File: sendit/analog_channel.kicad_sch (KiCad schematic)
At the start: 21 parts, among them J2 Conn_01x03, J4 JUMPER, J5 Conn_02x05_Odd_Even, J6 JUMPER, J7 Conn_02x05_Odd_Even, J8 JUMPER

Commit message: more work on rev c board schematic
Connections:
- net EXTERN renamed VEXT
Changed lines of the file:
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@@
 	(wire
 		(pts
-			(xy 85.09 60.96) (xy 85.09 71.12)
+			(xy 85.09 62.23) (xy 85.09 71.12)
 		)
 		(stroke
@@
 			(width 0)
 			(type default)
-		)
-	)
-	(global_label "EXTERN"
-		(shape input)
-		(at 85.09 60.96 90)
-		(fields_autoplaced yes)
-		(effects
-			(font
-				(size 1.27 1.27)
-			)
-			(justify left)
-		)
-		(property "Intersheetrefs" "${INTERSHEET_REFS}"
-			(at 85.09 50.8992 90)
-			(effects
-				(font
-					(size 1.27 1.27)
-				)
-				(justify left)
-			)
 		)
 	)
@@
 					(unit 1)
 				)
+			)
+		)
+	)
+	(symbol
+		(lib_id "power:VS")
+		(at 85.09 62.23 0)
+		(unit 1)
+		(exclude_from_sim no)
+		(in_bom yes)
+		(on_board yes)
+		(dnp no)
+		(fields_autoplaced yes)
+		(property "Reference" "#PWR0111"
+			(at 85.09 66.04 0)
+			(effects
+				(font
+					(size 1.27 1.27)
+				)
+				(hide yes)
+			)
+		)
+		(property "Value" "VEXT"
+			(at 85.09 57.15 0)
+			(effects
+				(font
+					(size 1.27 1.27)
+				)
+			)
+		)
+		(property "Footprint" ""
+			(at 85.09 62.23 0)
+			(effects
+				(font
+					(size 1.27 1.27)
+				)
+				(hide yes)
+			)
+		)
+		(property "Datasheet" ""
+			(at 85.09 62.23 0)
+			(effects
+				(font
+					(size 1.27 1.27)
+				)
+				(hide yes)
+			)
+		)
+		(property "Description" "Power symbol creates a global label with name \"VS\""
+			(at 85.09 62.23 0)
+			(effects
+				(font
+					(size 1.27 1.27)
+				)
+				(hide yes)
+			)
+		)
+		(pin "1"
+		)
+		(instances
+			(project "sendit"
+				(path "/a355e4d0-2918-44fc-be8d-2503b84c6d6c/06289466-09ce-4e8d-a3fe-f20bb105c2b9"
+					(reference "#PWR0114")
+					(unit 1)
+				)
+				(path "/a355e4d0-2918-44fc-be8d-2503b84c6d6c/5dcf4aa4-b4c0-4eb4-9810-8e1da6fba809"
+					(reference "#PWR0112")
+					(unit 1)
+				)
+				(path "/a355e4d0-2918-44fc-be8d-2503b84c6d6c/81493a67-66de-41a8-9145-e2b5bf5e8fe3"
+					(reference "#PWR0117")
+					(unit 1)
+				)
+				(path "/a355e4d0-2918-44fc-be8d-2503b84c6d6c/8214e645-c73d-48c5-bbb1-69f276b453fe"
+					(reference "#PWR0113")
+					(unit 1)
+				)
+				(path "/a355e4d0-2918-44fc-be8d-2503b84c6d6c/9719621a-b94a-4b2b-95d3-3cdc5abcb21e"
+					(reference "#PWR0118")
+					(unit 1)
+				)
+				(path "/a355e4d0-2918-44fc-be8d-2503b84c6d6c/d62eac9c-79f7-42c7-961a-243a4f5db43f"
+					(reference "#PWR0111")
+					(unit 1)
+				)
+				(path "/a355e4d0-2918-44fc-be8d-2503b84c6d6c/dea3d2e6-dd3a-44c1-a00c-3b7e188a1340"
+					(reference "#PWR0115")
+					(unit 1)
+				)
+				(path "/a355e4d0-2918-44fc-be8d-2503b84c6d6c/edcf8ea2-5577-432a-b9e3-a0cdd8283da4"
+					(reference "#PWR0116")
+					(unit 1)
+				)

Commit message: most of the work on the schematic is done.
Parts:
- renumbered TP1 to TP3, TP2 to TP4

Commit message: more work towards rev c board.
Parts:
- renumbered INPUT2 to INPUT1, J2 to J1, J3 to J2, J4 to J3, J5 to J4, J6 to J5, J7 to J6, J8 to J7, R1 to R3, R2 to R4, R3 to R5, R4 to R6, R5 to R7, R6 to R8, R7 to R9

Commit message: power system work and layout
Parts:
- renumbered J1 to J2, J2 to J3, J3 to J4, J4 to J5, J5 to J6, J6 to J7, J7 to J8

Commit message: big change removing the usb hub and serial chip.
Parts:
- renumbered J2 to J3, J3 to J4, J4 to J5, J5 to J6, J6 to J7, J7 to J8, J8 to J9

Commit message: big routing push
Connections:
- net +24V: now also J4.4 (Pin_4); no longer J4.6 (Pin_6)
- net +3.3VADC: now also J4.8 (Pin_8); no longer J4.2 (Pin_2)
- net +5V: now also J4.6 (Pin_6); no longer J4.4 (Pin_4)
- net VEXT: now also J4.2 (Pin_2); no longer J4.8 (Pin_8)
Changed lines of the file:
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@@
 	(wire
 		(pts
-			(xy 60.96 66.04) (xy 72.39 66.04)
+			(xy 60.96 66.04) (xy 71.12 66.04)
 		)
 		(stroke
@@
 	(wire
 		(pts
-			(xy 72.39 62.23) (xy 72.39 66.04)
+			(xy 71.12 62.23) (xy 71.12 66.04)
 		)
 		(stroke
@@
 	(wire
 		(pts
-			(xy 78.74 62.23) (xy 78.74 68.58)
+			(xy 77.47 62.23) (xy 77.47 68.58)
 		)
 		(stroke
@@
 	(wire
 		(pts
-			(xy 60.96 68.58) (xy 78.74 68.58)
+			(xy 60.96 68.58) (xy 77.47 68.58)
 		)
 		(stroke
@@
 	(symbol
 		(lib_id "power:+24V")
-		(at 78.74 62.23 0)
+		(at 71.12 62.23 0)
 		(unit 1)
 		(exclude_from_sim no)
@@
 		(fields_autoplaced yes)
 		(property "Reference" "#PWR019"
-			(at 78.74 66.04 0)
+			(at 71.12 66.04 0)
 			(effects
 				(font
@@
 		)
 		(property "Value" "+24V"
-			(at 78.74 57.15 0)
+			(at 71.12 57.15 0)
 			(effects
 				(font
@@
 		)
 		(property "Footprint" ""
-			(at 78.74 62.23 0)
+			(at 71.12 62.23 0)
 			(effects
 				(font
@@
 		)
 		(property "Datasheet" ""
-			(at 78.74 62.23 0)
+			(at 71.12 62.23 0)
 			(effects
 				(font
@@
 		)
 		(property "Description" "Power symbol creates a global label with name \"+24V\""
-			(at 78.74 62.23 0)
+			(at 71.12 62.23 0)
 			(effects
 				(font
@@
 	(symbol
 		(lib_id "power:+3.3VADC")
-		(at 64.77 62.23 0)
+		(at 85.09 62.23 0)
 		(mirror y)
 		(unit 1)
@@
 		(dnp no)
 		(property "Reference" "#PWR017"
-			(at 60.96 63.5 0)
+			(at 81.28 63.5 0)
 			(effects
 				(font
@@
 		)
 		(property "Value" "+3.3VADC"
-			(at 64.77 57.15 0)
+			(at 85.09 57.15 0)
 			(effects
 				(font
@@
 		)
 		(property "Footprint" ""
-			(at 64.77 62.23 0)
+			(at 85.09 62.23 0)
 			(effects
 				(font
@@
 		)
 		(property "Datasheet" ""
-			(at 64.77 62.23 0)
+			(at 85.09 62.23 0)
 			(effects
 				(font
@@
 		)
 		(property "Description" "Power symbol creates a global label with name \"+3.3VADC\""
-			(at 64.77 62.23 0)
+			(at 85.09 62.23 0)
 			(effects
 				(font
@@
 	(symbol
 		(lib_id "power:+5V")
-		(at 72.39 62.23 0)
+		(at 77.47 62.23 0)
 		(unit 1)
 		(exclude_from_sim no)
@@
 		(fields_autoplaced yes)
 		(property "Reference" "#PWR018"
-			(at 72.39 66.04 0)
+			(at 77.47 66.04 0)
 			(effects
 				(font
@@
 		)
 		(property "Value" "+5V"
-			(at 72.39 57.15 0)
+			(at 77.47 57.15 0)
 			(effects
 				(font
@@
 		)
 		(property "Footprint" ""
-			(at 72.39 62.23 0)
+			(at 77.47 62.23 0)
 			(effects
 				(font
@@
 		)
 		(property "Datasheet" ""
-			(at 72.39 62.23 0)
+			(at 77.47 62.23 0)
 			(effects
 				(font
@@
 		)
 		(property "Description" "Power symbol creates a global label with name \"+5V\""
-			(at 72.39 62.23 0)
+			(at 77.47 62.23 0)
 			(effects
 				(font
@@
 	(symbol
 		(lib_id "power:VS")
-		(at 85.09 62.23 0)
+		(at 64.77 62.23 0)
 		(unit 1)
 		(exclude_from_sim no)
@@
 		(fields_autoplaced yes)
 		(property "Reference" "#PWR020"
-			(at 85.09 66.04 0)
+			(at 64.77 66.04 0)
 			(effects
 				(font
@@
 		)
 		(property "Value" "VEXT"
-			(at 85.09 57.15 0)
+			(at 64.77 57.15 0)
 			(effects
 				(font
@@
 		)
 		(property "Footprint" ""
-			(at 85.09 62.23 0)
+			(at 64.77 62.23 0)
 			(effects
 				(font
@@
 		)
 		(property "Datasheet" ""
-			(at 85.09 62.23 0)
+			(at 64.77 62.23 0)
 			(effects
 				(font
@@
 		)
 		(property "Description" "Power symbol creates a global label with name \"VS\""
-			(at 85.09 62.23 0)
+			(at 64.77 62.23 0)
 			(effects
 				(font

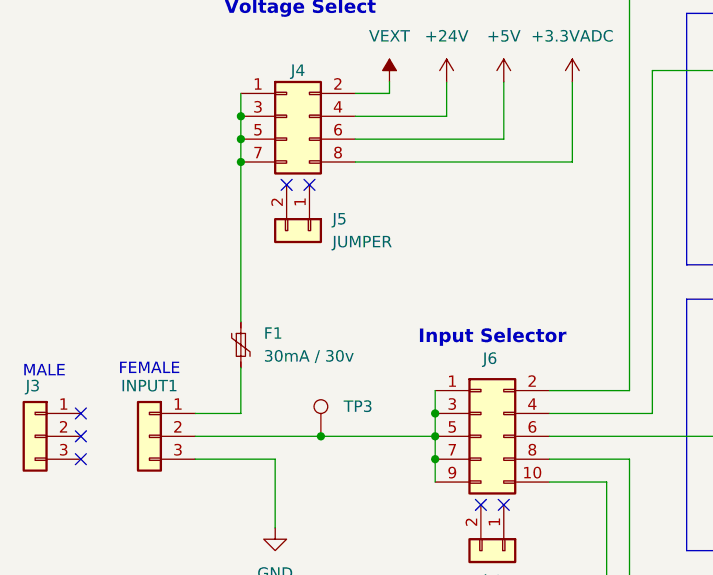
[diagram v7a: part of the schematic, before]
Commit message: via stitching and calculations
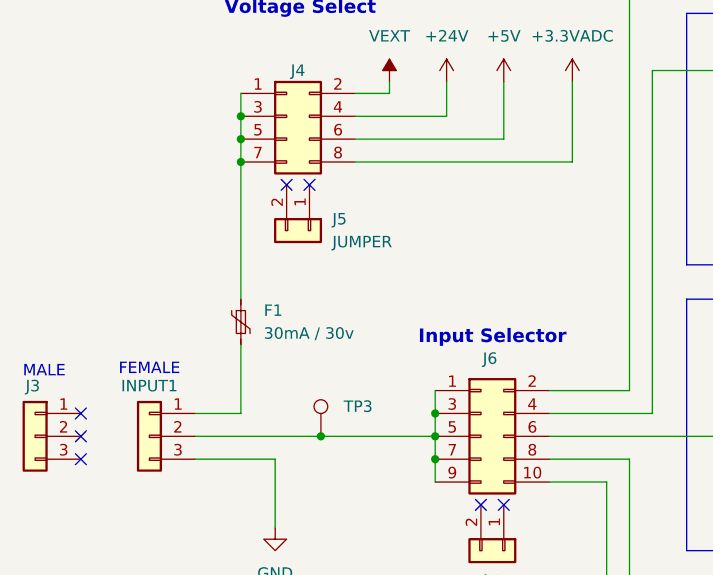
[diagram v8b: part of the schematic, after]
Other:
- moved on the sheet: F1
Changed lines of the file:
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@@
 	(wire
 		(pts
-			(xy 48.26 71.12) (xy 48.26 88.9)
+			(xy 48.26 71.12) (xy 48.26 86.36)
 		)
 		(stroke
@@
 	(wire
 		(pts
-			(xy 48.26 93.98) (xy 48.26 99.06)
+			(xy 48.26 91.44) (xy 48.26 99.06)
 		)
 		(stroke
@@
 	(symbol
 		(lib_id "Device:Polyfuse_Small")
-		(at 48.26 91.44 0)
+		(at 48.26 88.9 0)
 		(unit 1)
 		(exclude_from_sim no)
@@
 		(fields_autoplaced yes)
 		(property "Reference" "F1"
-			(at 50.8 90.1699 0)
+			(at 50.8 87.6299 0)
 			(effects
 				(font
@@
 		)
 		(property "Value" "30mA / 30v"
-			(at 50.8 92.7099 0)
+			(at 50.8 90.1699 0)
 			(effects
 				(font
@@
 		)
 		(property "Footprint" "Fuse:Fuse_0603_1608Metric"
-			(at 49.53 96.52 0)
+			(at 49.53 93.98 0)
 			(effects
 				(font
@@
 		)
 		(property "Datasheet" "~"
-			(at 48.26 91.44 0)
+			(at 48.26 88.9 0)
 			(effects
 				(font
@@
 		)
 		(property "Description" "Resettable fuse, polymeric positive temperature coefficient, small symbol"
-			(at 48.26 91.44 0)
+			(at 48.26 88.9 0)
 			(effects
 				(font
@@
 		)
 		(property "LCSC" "C2687870"
-			(at 48.26 91.44 0)
+			(at 48.26 88.9 0)
 			(effects
 				(font
@@
 		)
 		(property "LCSC Part Name" ""
-			(at 48.26 91.44 0)
+			(at 48.26 88.9 0)
 			(effects
 				(font
@@
 		)
 		(property "Manufacturer" ""
-			(at 48.26 91.44 0)
+			(at 48.26 88.9 0)
 			(effects
 				(font
@@
 		)
 		(property "Manufacturer Part" ""
-			(at 48.26 91.44 0)
+			(at 48.26 88.9 0)
 			(effects
 				(font
@@
 		)
 		(property "Supplier" ""
-			(at 48.26 91.44 0)
+			(at 48.26 88.9 0)
 			(effects
 				(font
@@
 		)
 		(property "Supplier Part" ""
-			(at 48.26 91.44 0)
+			(at 48.26 88.9 0)
 			(effects
 				(font
@@
 					(size 1.27 1.27)
 				)
+				(hide yes)
 			)
 		)
